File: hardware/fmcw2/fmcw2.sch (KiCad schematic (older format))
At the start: 136 parts, among them P1 CONN_15X2, Q1 SSM3K15AFS, U1 ADF4158, U10 HMC431LP4, U11 SKY65404, U12 PAT1220-6dB, U13 SMA, U14 MGA-25203, U15 SMA, U16 HMC313, U19 LDS3985, U2 SG-210STF 30MHz, U3 PAT1220-6dB, U4 5400BL15B050E, U5 LT6232, U6 ADL5801, U7 TLV271, U8 5400BL15B050E, U9 MCP1700

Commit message: Rescue schematic symbols to a new library
Schematic used old symbols and without cached library files
uses instead the new symbols that have different pin pitch.
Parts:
- C1, C10, C11, C12, C13, C14, C15, C16, C17, C18, C19, C2, C20, C21, C22, C24, C25, C26, C27, C28, C29, C3, C30, C31, C32, C33, C34, C35, C36, C37, C38, C39, C4, C40, C41, C42, C43, C44, C47, C48, C49, C5, C50, C51, C52, C53, C54, C55, C56, C57, C58, C59, C6, C60, C61, C62, C64, C65, C66, C67, C68, C7, C8, C9: symbol C -> C-RESCUE-fmcw2
- D1: symbol LED -> LED-RESCUE-fmcw2
- R1, R10, R11, R12, R13, R14, R15, R16, R17, R18, R19, R2, R20, R21, R22, R23, R24, R25, R26, R27, R28, R29, R3, R30, R31, R32, R33, R34, R35, R36, R37, R38, R39, R4, R40, R5, R6, R7, R8, R9: symbol R -> R-RESCUE-fmcw2

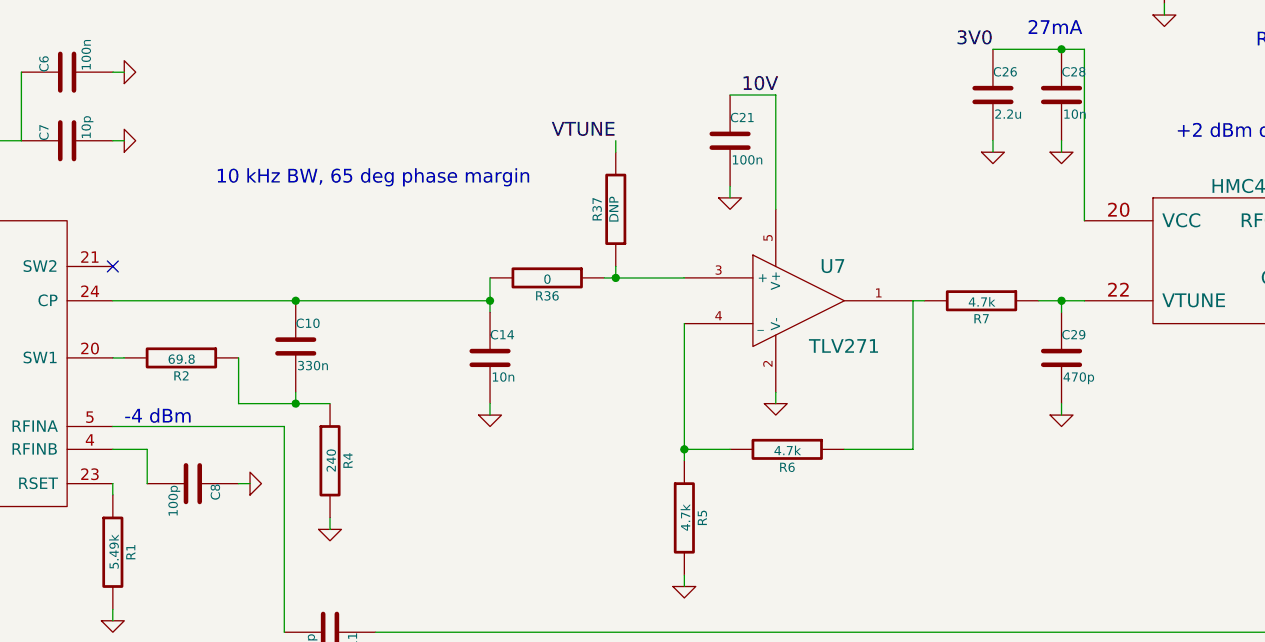
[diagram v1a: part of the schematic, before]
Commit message: Increase PLL loop bandwidth
Faster frequency settling
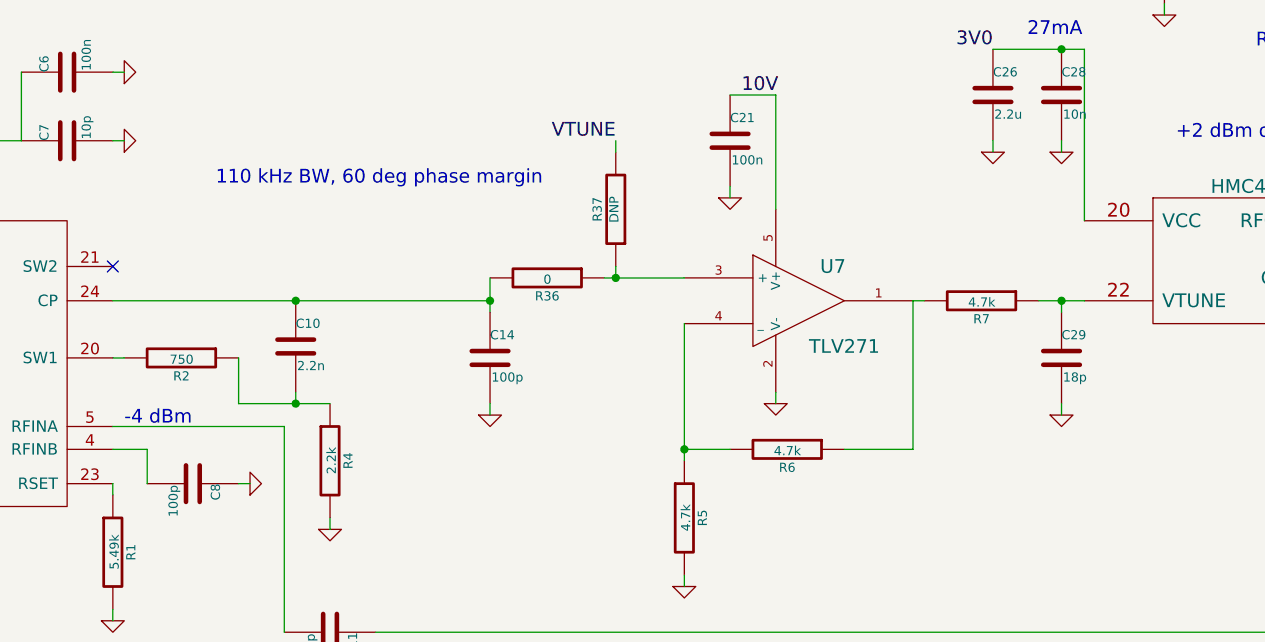
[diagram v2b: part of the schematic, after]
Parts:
- C10: value 330n -> 2.2n
- C14: value 10n -> 100p
- C29: value 470p -> 18p
- R2: value 69.8 -> 750
- R4: value 240 -> 2.2k
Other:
- note added: "110 kHz BW, 60 deg phase margin"
- note removed: "10 kHz BW, 65 deg phase margin"
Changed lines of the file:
@@
 P 4950 3650
 F 0 "C10" H 4950 3750 40  0000 L CNN
-F 1 "330n" H 4956 3565 40  0000 L CNN
+F 1 "2.2n" H 4956 3565 40  0000 L CNN
 F 2 "fmcw2:C_0402b" H 4988 3500 30  0001 C CNN
 F 3 "" H 4950 3650 60  0000 C CNN
@@
 P 4450 3700
 F 0 "R2" V 4530 3700 40  0000 C CNN
-F 1 "69.8" V 4457 3701 40  0000 C CNN
+F 1 "750" V 4457 3701 40  0000 C CNN
 F 2 "fmcw2:R_0402b" V 4380 3700 30  0001 C CNN
 F 3 "" H 4450 3700 30  0000 C CNN
@@
 P 5100 4150
 F 0 "R4" V 5180 4150 40  0000 C CNN
-F 1 "240" V 5107 4151 40  0000 C CNN
+F 1 "2.2k" V 5107 4151 40  0000 C CNN
 F 2 "fmcw2:R_0402b" V 5030 4150 30  0001 C CNN
 F 3 "" H 5100 4150 30  0000 C CNN
@@
 P 8300 3700
 F 0 "C29" H 8300 3800 40  0000 L CNN
-F 1 "470p" H 8306 3615 40  0000 L CNN
+F 1 "18p" H 8306 3615 40  0000 L CNN
 F 2 "fmcw2:C_0402b" H 8338 3550 30  0001 C CNN
 F 3 "" H 8300 3700 60  0000 C CNN
@@
 P 5800 3700
 F 0 "C14" H 5800 3800 40  0000 L CNN
-F 1 "10n" H 5806 3615 40  0000 L CNN
+F 1 "100p" H 5806 3615 40  0000 L CNN
 F 2 "fmcw2:C_0402b" H 5838 3550 30  0001 C CNN
 F 3 "" H 5800 3700 60  0000 C CNN
@@
 ADF_MUXOUT
 Text Notes 4600 2950 0    60   ~ 0
-10 kHz BW, 65 deg phase margin
+110 kHz BW, 60 deg phase margin
 $Comp
 L SG-210STF U2
